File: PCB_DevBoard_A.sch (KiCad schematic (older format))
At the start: 49 parts, among them J1 Interconnect B, J2 Interconnect A, J3 Debug, J5 I/O A, J6 I/O B, SW1 SW_DPST_x2, U1 TLV1117-33, U2 XMC1404_F064, U3 TLE7251, U4 ULN2003A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

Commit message: Rescue
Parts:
- SW1: symbol Switch:SW_DPST_x2 -> PCB_DevBoard_A-rescue:SW_DPST_x2-Switch
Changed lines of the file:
@@
 EESchema Schematic File Version 4
-LIBS:PCB_DevBoard_A-cache
-EELAYER 29 0
+EELAYER 30 0
 EELAYER END
 $Descr A3 16535 11693
@@
 NoConn ~ 13200 4550
 $Comp
-L Switch:SW_DPST_x2 SW1
+L PCB_DevBoard_A-rescue:SW_DPST_x2-Switch SW1
 U 1 1 5F3F7356
 P 12300 7700

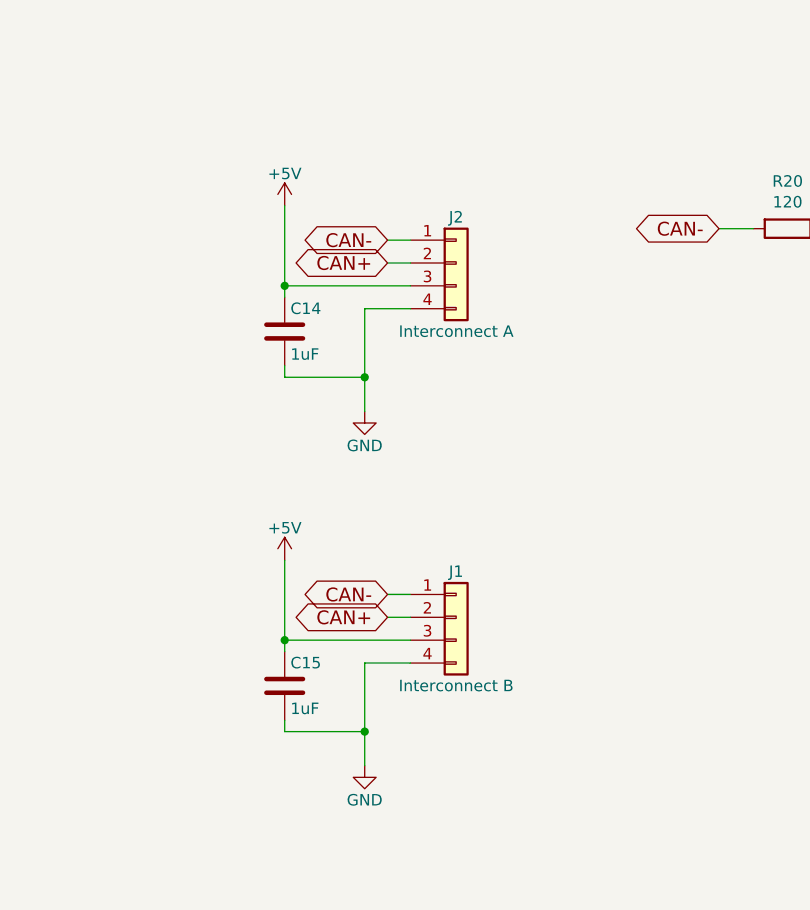
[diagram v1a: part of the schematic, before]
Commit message: Change the Wolley connectors to the new 5-pin one
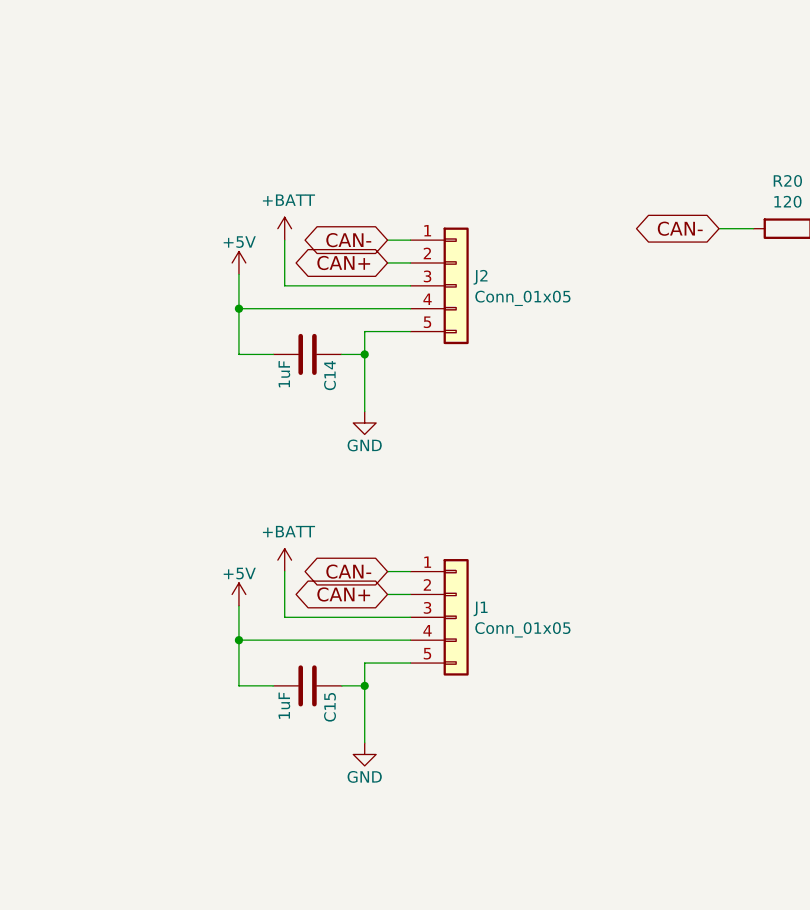
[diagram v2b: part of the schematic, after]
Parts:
- removed J1: Interconnect B, DevBoard:WolletInterconnect_THT_Angeled, symbol PCB_DevBoard_A-rescue:Conn_01x04
- removed J2: Interconnect A, DevBoard:WolletInterconnect_THT_Angeled, symbol PCB_DevBoard_A-rescue:Conn_01x04
- added J1, J2: Conn_01x05, DevBoard:WolleyInterconnect_THT_Angeled, symbol Connector_Generic:Conn_01x05
- C15: footprint Capacitors_SMD:C_0805_HandSoldering -> Capacitor_SMD:C_0805_2012Metric_Pad1.18x1.45mm_HandSolder
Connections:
- net +5V: now also C14.2, C15.2, J1.4 (Pin_4), J2.4 (Pin_4); no longer C14.1, C15.1
- net CAN+: now also J1.2 (Pin_2), J2.2 (Pin_2)
- net CAN-: now also J1.1 (Pin_1), J2.1 (Pin_1)
- net GND: now also C14.1, C15.1, J1.5 (Pin_5), J2.5 (Pin_5); no longer C14.2, C15.2
- new net +BATT: J1.3 (Pin_3), J2.3 (Pin_3)
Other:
- moved on the sheet: C14
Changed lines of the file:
@@
-$EndComp
-$Comp
-L PCB_DevBoard_A-rescue:Conn_01x04 J1
-U 1 1 5C167076
-P 10350 9400
-F 0 "J1" H 10350 9600 50  0000 C CNN
-F 1 "Interconnect B" H 10350 9100 50  0000 C CNN
-F 2 "DevBoard:WolletInterconnect_THT_Angeled" H 10350 9400 50  0001 C CNN
-F 3 "" H 10350 9400 50  0001 C CNN
-	1    10350 9400
-	1    0    0    -1
 $EndComp
 $Comp
@@
 	2900 1550 2900 1750
 Connection ~ 3200 1550
-Text GLabel 10050 9300 0    60   BiDi ~ 0
-CAN-
-Text GLabel 10050 9400 0    60   BiDi ~ 0
-CAN+
-$Comp
-L PCB_DevBoard_A-rescue:GND #PWR06
-U 1 1 5C168105
-P 9950 10050
-F 0 "#PWR06" H 9950 9800 50  0001 C CNN
-F 1 "GND" H 9950 9900 50  0000 C CNN
-F 2 "" H 9950 10050 50  0001 C CNN
-F 3 "" H 9950 10050 50  0001 C CNN
-	1    9950 10050
-	1    0    0    -1
-$EndComp
-$Comp
-L PCB_DevBoard_A-rescue:+5V #PWR03
-U 1 1 5C16818E
-P 9600 9150
-F 0 "#PWR03" H 9600 9000 50  0001 C CNN
-F 1 "+5V" H 9600 9290 50  0000 C CNN
-F 2 "" H 9600 9150 50  0001 C CNN
-F 3 "" H 9600 9150 50  0001 C CNN
-	1    9600 9150
-	1    0    0    -1
-$EndComp
-Wire Wire Line
-	10150 9600 9950 9600
-Wire Wire Line
-	9950 9600 9950 9900
-Wire Wire Line
-	10150 9500 9600 9500
-Wire Wire Line
-	9600 9500 9600 9150
-Wire Wire Line
-	10150 9300 10050 9300
-Wire Wire Line
-	10050 9400 10150 9400
-$Comp
-L PCB_DevBoard_A-rescue:Conn_01x04 J2
-U 1 1 5C168384
-P 10350 7850
-F 0 "J2" H 10350 8050 50  0000 C CNN
-F 1 "Interconnect A" H 10350 7550 50  0000 C CNN
-F 2 "DevBoard:WolletInterconnect_THT_Angeled" H 10350 7850 50  0001 C CNN
-F 3 "" H 10350 7850 50  0001 C CNN
-	1    10350 7850
-	1    0    0    -1
-$EndComp
 Text GLabel 10050 7750 0    60   BiDi ~ 0
 CAN-
@@
 L PCB_DevBoard_A-rescue:+5V #PWR04
 U 1 1 5C168392
-P 9600 7600
-F 0 "#PWR04" H 9600 7450 50  0001 C CNN
-F 1 "+5V" H 9600 7740 50  0000 C CNN
-F 2 "" H 9600 7600 50  0001 C CNN
-F 3 "" H 9600 7600 50  0001 C CNN
-	1    9600 7600
-	1    0    0    -1
-$EndComp
-Wire Wire Line
-	10150 8050 9950 8050
-Wire Wire Line
-	9950 8050 9950 8350
-Wire Wire Line
-	10150 7950 9600 7950
-Wire Wire Line
-	9600 7950 9600 7600
+P 9400 7900
+F 0 "#PWR04" H 9400 7750 50  0001 C CNN
+F 1 "+5V" H 9400 8040 50  0000 C CNN
+F 2 "" H 9400 7900 50  0001 C CNN
+F 3 "" H 9400 7900 50  0001 C CNN
+	1    9400 7900
+	1    0    0    -1
+$EndComp
 Wire Wire Line
 	10150 7750 10050 7750
@@
 L PCB_DevBoard_A-rescue:C C14
 U 1 1 5F297810
-P 9600 8150
-F 0 "C14" H 9625 8250 50  0000 L CNN
-F 1 "1uF" H 9625 8050 50  0000 L CNN
-F 2 "Capacitors_SMD:C_0805_HandSoldering" H 9638 8000 50  0001 C CNN
-F 3 "" H 9600 8150 50  0001 C CNN
-	1    9600 8150
-	1    0    0    -1
-$EndComp
-$Comp
-L PCB_DevBoard_A-rescue:C C15
-U 1 1 5F297D17
-P 9600 9700
-F 0 "C15" H 9625 9800 50  0000 L CNN
-F 1 "1uF" H 9625 9600 50  0000 L CNN
-F 2 "Capacitors_SMD:C_0805_HandSoldering" H 9638 9550 50  0001 C CNN
-F 3 "" H 9600 9700 50  0001 C CNN
-	1    9600 9700
-	1    0    0    -1
+P 9700 8250
+F 0 "C14" H 9725 8350 50  0000 L CNN
+F 1 "1uF" H 9725 8150 50  0000 L CNN
+F 2 "Capacitors_SMD:C_0805_HandSoldering" H 9738 8100 50  0001 C CNN
+F 3 "" H 9700 8250 50  0001 C CNN
+	1    9700 8250
+	0    1    1    0
 $EndComp
 $Comp
@@
 Wire Wire Line
 	14550 2050 14400 2050
-Wire Wire Line
-	9600 8000 9600 7950
-Connection ~ 9600 7950
-Wire Wire Line
-	9600 8300 9600 8350
-Wire Wire Line
-	9600 8350 9950 8350
-Connection ~ 9950 8350
-Wire Wire Line
-	9950 8350 9950 8500
-Wire Wire Line
-	9600 9550 9600 9500
-Connection ~ 9600 9500
-Wire Wire Line
-	9600 9850 9600 9900
-Wire Wire Line
-	9600 9900 9950 9900
-Connection ~ 9950 9900
-Wire Wire Line
-	9950 9900 9950 10050
 Wire Wire Line
 	7350 9950 7350 10050
@@
 Wire Wire Line
 	6800 4350 7950 4350
+$Comp
+L Connector_Generic:Conn_01x05 J2
+U 1 1 6406ABD3
+P 10350 7950
+F 0 "J2" H 10430 7992 50  0000 L CNN
+F 1 "Conn_01x05" H 10430 7901 50  0000 L CNN
+F 2 "DevBoard:WolleyInterconnect_THT_Angeled" H 10350 7950 50  0001 C CNN
+F 3 "~" H 10350 7950 50  0001 C CNN
+	1    10350 7950
+	1    0    0    -1
+$EndComp
+Wire Wire Line
+	9400 7900 9400 8050
+Wire Wire Line
+	9950 8150 10150 8150
+Wire Wire Line
+	10150 8050 9400 8050
+$Comp
+L power:+BATT #PWR0105
+U 1 1 64106B30
+P 9600 7750
+F 0 "#PWR0105" H 9600 7600 50  0001 C CNN
+F 1 "+BATT" H 9615 7923 50  0000 C CNN
+F 2 "" H 9600 7750 50  0001 C CNN
+F 3 "" H 9600 7750 50  0001 C CNN
+	1    9600 7750
+	1    0    0    -1
+$EndComp
+Wire Wire Line
+	10150 7950 9600 7950
+Wire Wire Line
+	9600 7950 9600 7750
+Wire Wire Line
+	9950 8150 9950 8250
+Wire Wire Line
+	9850 8250 9950 8250
+Connection ~ 9950 8250
+Wire Wire Line
+	9950 8250 9950 8500
+Wire Wire Line
+	9550 8250 9400 8250
+Wire Wire Line
+	9400 8250 9400 8050
+Connection ~ 9400 8050
+Text GLabel 10050 9200 0    60   BiDi ~ 0
+CAN-
+Text GLabel 10050 9300 0    60   BiDi ~ 0
+CAN+
+$Comp
+L PCB_DevBoard_A-rescue:GND #PWR0106
+U 1 1 642032D2
+P 9950 9950
+F 0 "#PWR0106" H 9950 9700 50  0001 C CNN
+F 1 "GND" H 9950 9800 50  0000 C CNN
+F 2 "" H 9950 9950 50  0001 C CNN
+F 3 "" H 9950 9950 50  0001 C CNN
+	1    9950 9950
+	1    0    0    -1
+$EndComp
+$Comp
+L PCB_DevBoard_A-rescue:+5V #PWR0107
+U 1 1 642032DC
+P 9400 9350
+F 0 "#PWR0107" H 9400 9200 50  0001 C CNN
+F 1 "+5V" H 9400 9490 50  0000 C CNN
+F 2 "" H 9400 9350 50  0001 C CNN
+F 3 "" H 9400 9350 50  0001 C CNN
+	1    9400 9350
+	1    0    0    -1
+$EndComp
+Wire Wire Line
+	10150 9200 10050 9200
+Wire Wire Line
+	10050 9300 10150 9300
+$Comp
+L PCB_DevBoard_A-rescue:C C15
+U 1 1 642032E8
+P 9700 9700
+F 0 "C15" H 9725 9800 50  0000 L CNN
+F 1 "1uF" H 9725 9600 50  0000 L CNN
+F 2 "Capacitor_SMD:C_0805_2012Metric_Pad1.18x1.45mm_HandSolder" H 9738 9550 50  0001 C CNN
+F 3 "" H 9700 9700 50  0001 C CNN
+	1    9700 9700
+	0    1    1    0
+$EndComp
+$Comp
+L Connector_Generic:Conn_01x05 J1
+U 1 1 642032F2
+P 10350 9400
+F 0 "J1" H 10430 9442 50  0000 L CNN
+F 1 "Conn_01x05" H 10430 9351 50  0000 L CNN
+F 2 "DevBoard:WolleyInterconnect_THT_Angeled" H 10350 9400 50  0001 C CNN
+F 3 "~" H 10350 9400 50  0001 C CNN
+	1    10350 9400
+	1    0    0    -1
+$EndComp
+Wire Wire Line
+	9400 9350 9400 9500
+Wire Wire Line
+	9950 9600 10150 9600
+Wire Wire Line
+	10150 9500 9400 9500
+$Comp
+L power:+BATT #PWR0108
+U 1 1 642032FF
+P 9600 9200
+F 0 "#PWR0108" H 9600 9050 50  0001 C CNN
+F 1 "+BATT" H 9615 9373 50  0000 C CNN
+F 2 "" H 9600 9200 50  0001 C CNN
+F 3 "" H 9600 9200 50  0001 C CNN
+	1    9600 9200
+	1    0    0    -1
+$EndComp
+Wire Wire Line
+	10150 9400 9600 9400
+Wire Wire Line
+	9600 9400 9600 9200
+Wire Wire Line
+	9950 9600 9950 9700
+Wire Wire Line
+	9850 9700 9950 9700
+Connection ~ 9950 9700
+Wire Wire Line
+	9950 9700 9950 9950
+Wire Wire Line
+	9550 9700 9400 9700
+Wire Wire Line
+	9400 9700 9400 9500
+Connection ~ 9400 9500
 $EndSCHEMATC

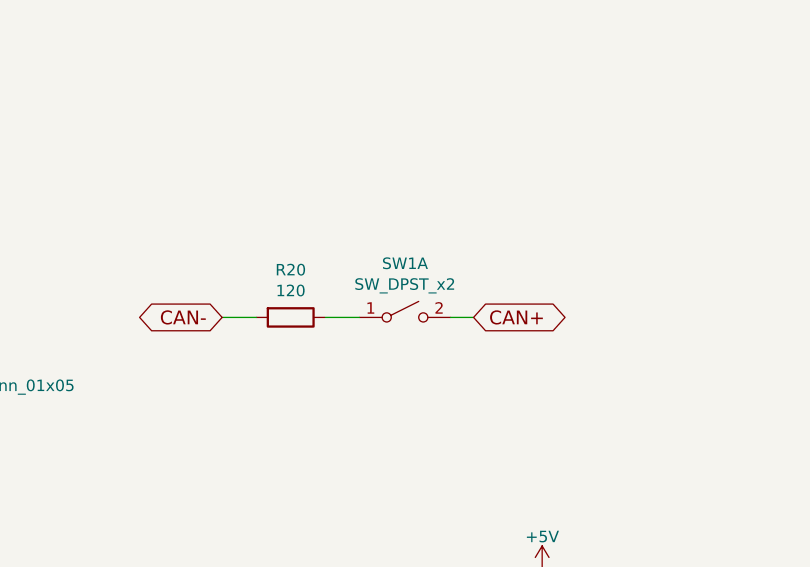
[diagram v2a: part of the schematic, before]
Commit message: Replace the termination switch with a jumper
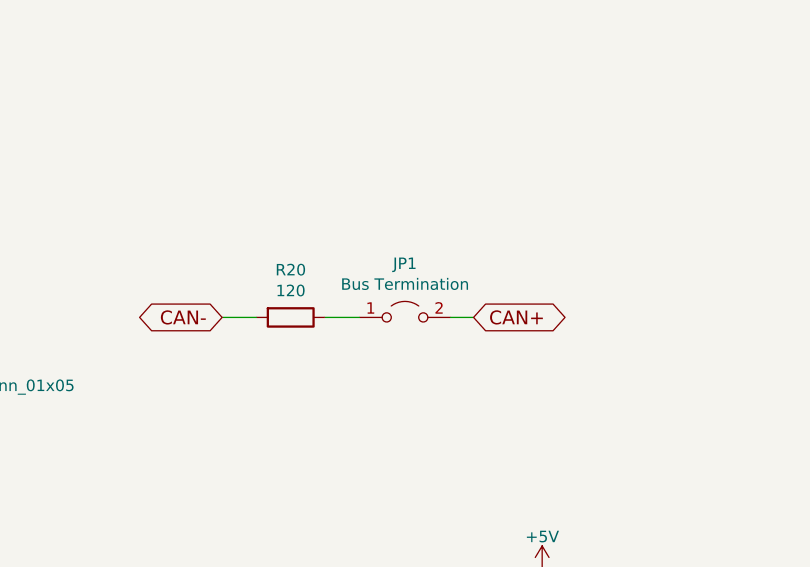
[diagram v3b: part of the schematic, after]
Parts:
- removed SW1: SW_DPST_x2, Pin_Headers:Pin_Header_Angled_1x03_Pitch2.54mm, symbol PCB_DevBoard_A-rescue:SW_DPST_x2-Switch
- added JP1: Bus Termination, Connector_PinHeader_2.54mm:PinHeader_1x02_P2.54mm_Vertical, symbol Jumper:Jumper_2_Open
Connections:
- net CAN+: now also JP1.2 (B)
- net at R20.1: now also JP1.1 (A)
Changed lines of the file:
@@
 NoConn ~ 13200 4550
-$Comp
-L PCB_DevBoard_A-rescue:SW_DPST_x2-Switch SW1
-U 1 1 5F3F7356
-P 12300 7700
-F 0 "SW1" H 12300 7935 50  0000 C CNN
-F 1 "SW_DPST_x2" H 12300 7844 50  0000 C CNN
-F 2 "Pin_Headers:Pin_Header_Angled_1x03_Pitch2.54mm" H 12300 7700 50  0001 C CNN
-F 3 "~" H 12300 7700 50  0001 C CNN
-	1    12300 7700
-	1    0    0    -1
-$EndComp
 $Comp
 L Device:R R20
@@
 	9400 9700 9400 9500
 Connection ~ 9400 9500
+$Comp
+L Jumper:Jumper_2_Open JP1
+U 1 1 64060E46
+P 12300 7700
+F 0 "JP1" H 12300 7935 50  0000 C CNN
+F 1 "Bus Termination" H 12300 7844 50  0000 C CNN
+F 2 "Connector_PinHeader_2.54mm:PinHeader_1x02_P2.54mm_Vertical" H 12300 7700 50  0001 C CNN
+F 3 "~" H 12300 7700 50  0001 C CNN
+	1    12300 7700
+	1    0    0    -1
+$EndComp
 $EndSCHEMATC
